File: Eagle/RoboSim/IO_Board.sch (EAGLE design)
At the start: 66 parts, among them IC1 74HC595N, IC2 74LS165N, IC3 74HC595N, IC4 74HC595N, IC5 OPAMP-DUALDIP

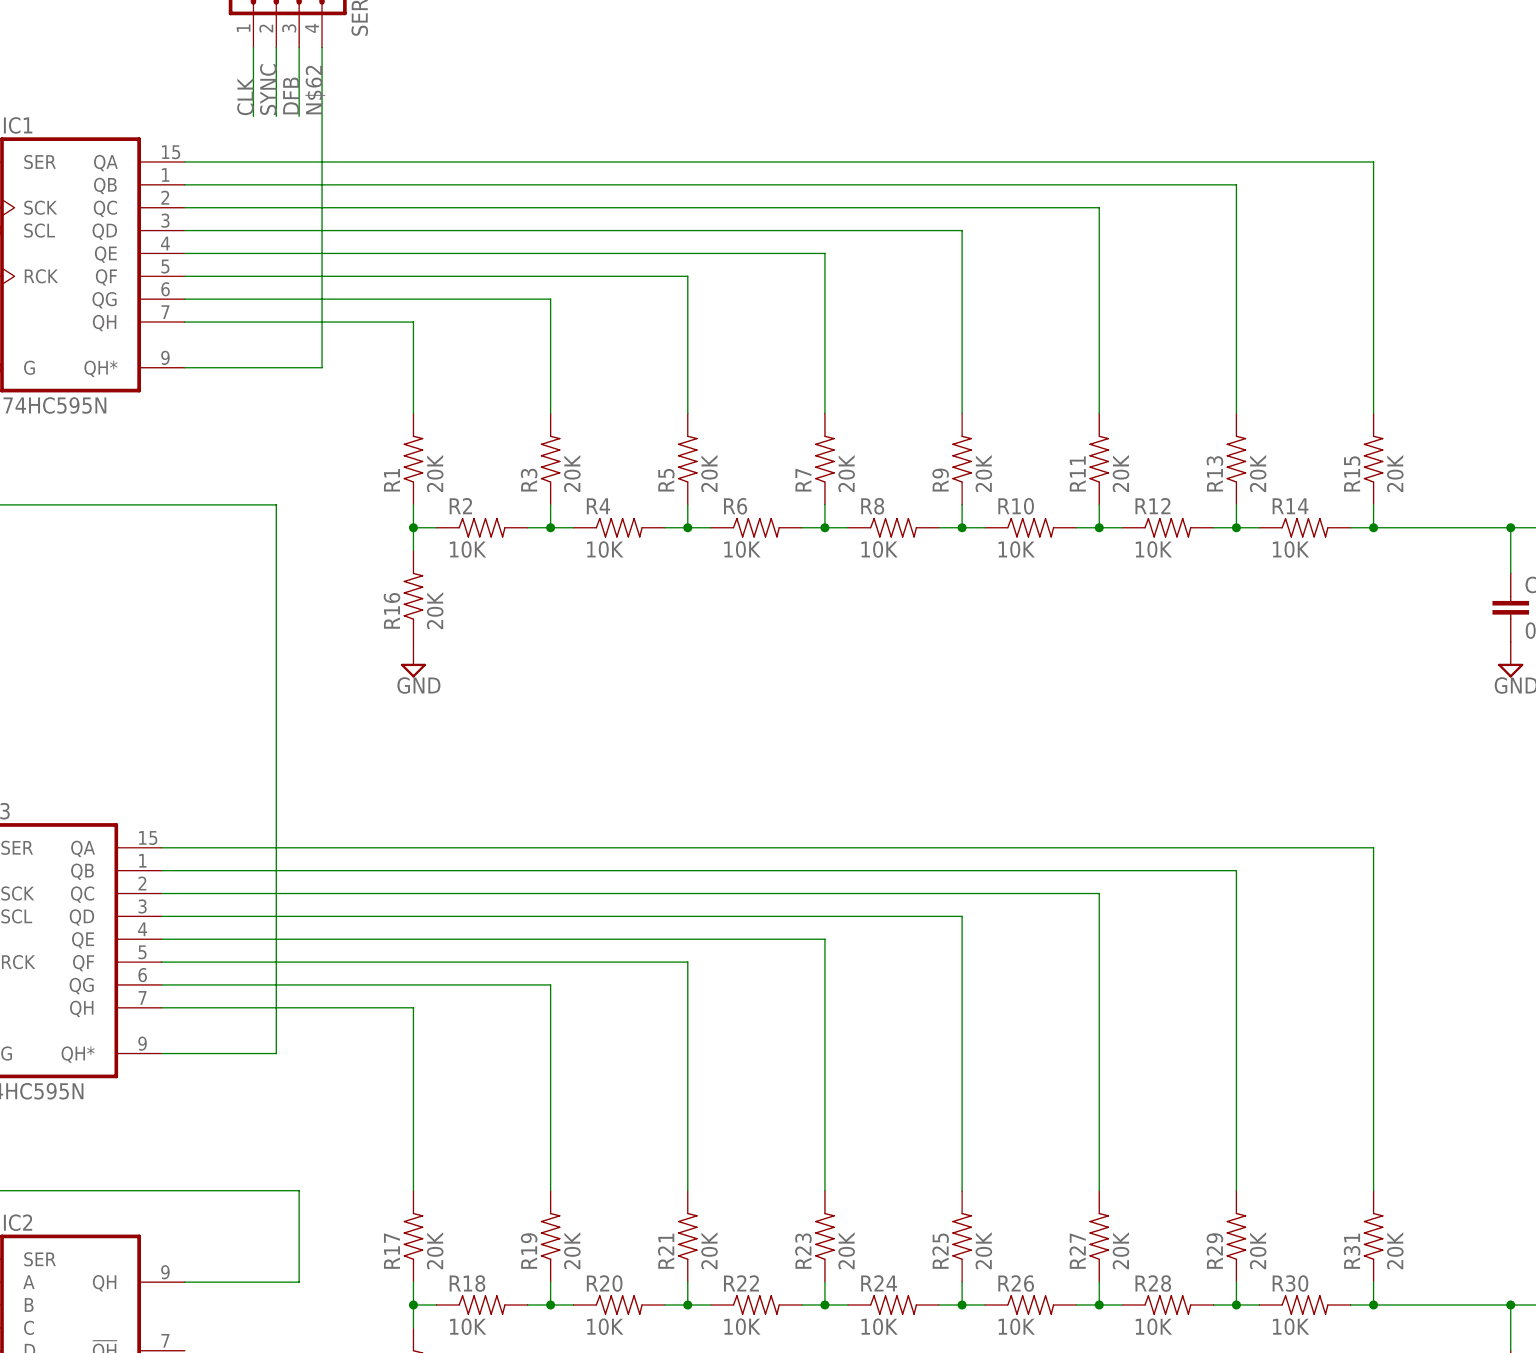
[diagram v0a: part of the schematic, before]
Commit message: updated wiring diagram for DAC's. added fast io functions to arduino code. Added test vector generation. Still tuning good compromise between signal fedility and processor load
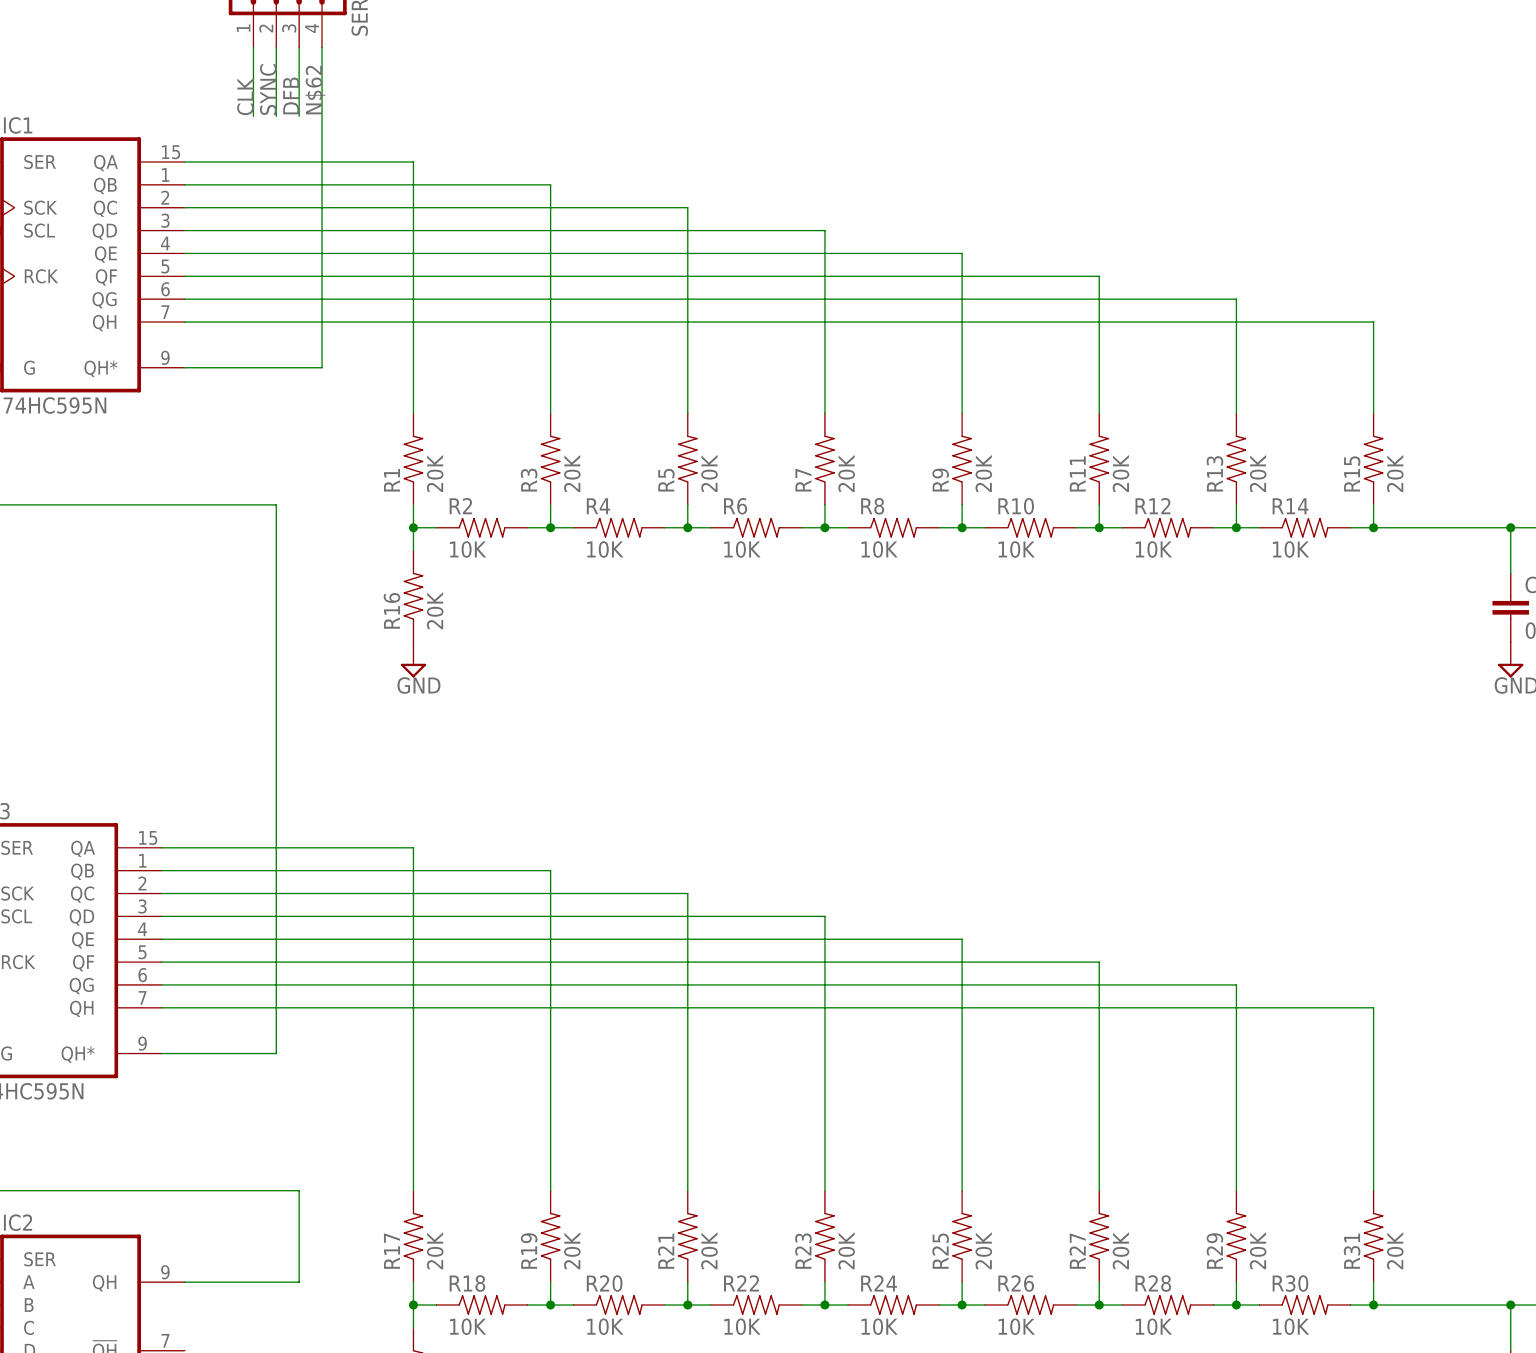
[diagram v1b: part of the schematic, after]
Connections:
- net N$1: now also IC1A.QH; no longer IC1A.QA
- net N$19: now also IC3A.QH; no longer IC3A.QA
- net N$20: now also IC3A.QG; no longer IC3A.QB
- net N$21: now also IC3A.QF; no longer IC3A.QC
- net N$22: now also IC3A.QE; no longer IC3A.QD
- net N$23: now also IC3A.QD; no longer IC3A.QE
- net N$24: now also IC3A.QC; no longer IC3A.QF
- net N$25: now also IC3A.QB; no longer IC3A.QG
- net N$26: now also IC3A.QA; no longer IC3A.QH
- net N$3: now also IC1A.QG; no longer IC1A.QB
- net N$4: now also IC1A.QF; no longer IC1A.QC
- net N$5: now also IC1A.QE; no longer IC1A.QD
- net N$6: now also IC1A.QD; no longer IC1A.QE
- net N$7: now also IC1A.QC; no longer IC1A.QF
- net N$8: now also IC1A.QB; no longer IC1A.QG
- net N$9: now also IC1A.QA; no longer IC1A.QH
